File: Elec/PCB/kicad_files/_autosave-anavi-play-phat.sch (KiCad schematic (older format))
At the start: 8 parts

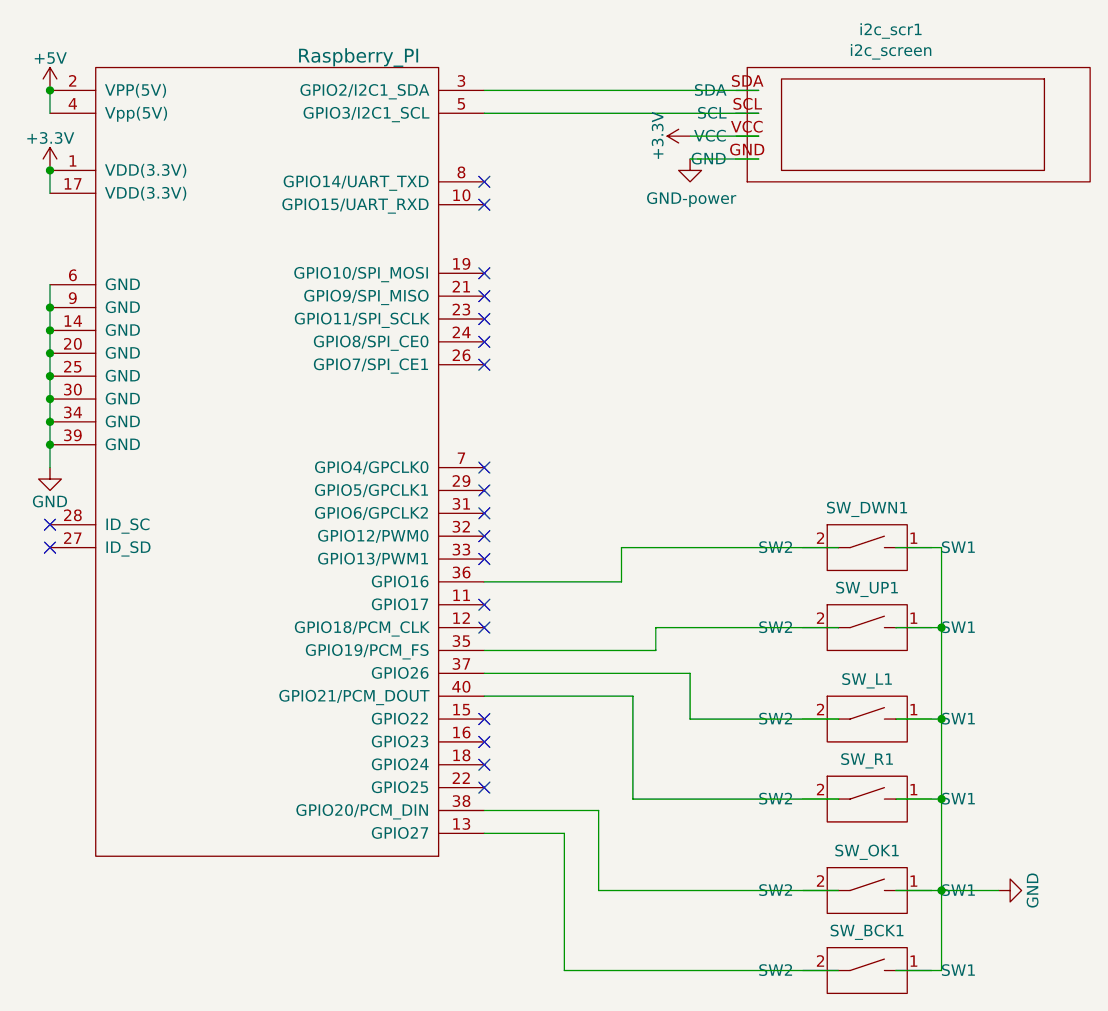
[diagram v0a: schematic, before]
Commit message: PCB v3 correction USB
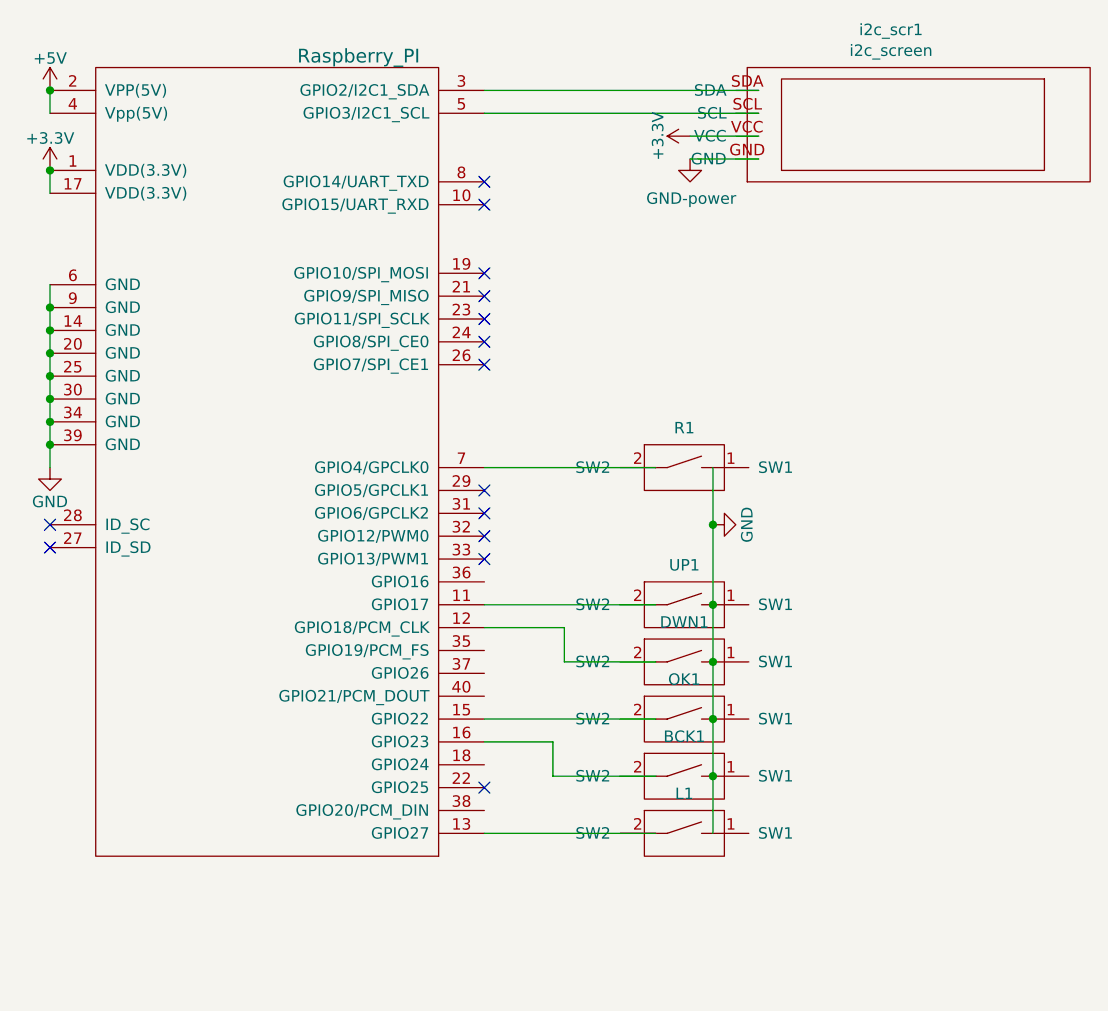
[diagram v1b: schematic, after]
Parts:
- removed SW_BCK1, SW_DWN1, SW_L1, SW_OK1, SW_R1: boutton_5mx5m, boutton:boutton__5mx5m, symbol boutton:boutton_5mx5m
- removed SW_UP1: boutton_5mx5, boutton:boutton__5mx5m, symbol boutton:boutton_5mx5m
- added BCK1, DWN1, L1, OK1, R1, UP1: boutton_6mx6m, boutton:boutton__6mx6m, symbol boutton:boutton_6mx6m
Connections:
- net GND: now also BCK1.1 (SW1), DWN1.1 (SW1), L1.1 (SW1), OK1.1 (SW1), R1.1 (SW1), UP1.1 (SW1)
- net at RASP_CONN1.11 (GPIO17): now also UP1.2 (SW2)
- net at RASP_CONN1.12 (GPIO18/PCM_CLK): now also DWN1.2 (SW2)
- net at RASP_CONN1.13 (GPIO27): now also L1.2 (SW2)
- net at RASP_CONN1.15 (GPIO22): now also OK1.2 (SW2)
- net at RASP_CONN1.16 (GPIO23): now also BCK1.2 (SW2)
- net at RASP_CONN1.7 (GPIO4/GPCLK0): now also R1.2 (SW2)
- no-connect marks 20 -> 14
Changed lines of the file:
@@
 $EndComp
 NoConn ~ 5350 4850
-NoConn ~ 5350 4750
-NoConn ~ 5350 4650
 NoConn ~ 5350 3750
 NoConn ~ 5350 2900
 NoConn ~ 5350 3000
-NoConn ~ 5350 4150
 NoConn ~ 5350 3850
 NoConn ~ 5350 2600
@@
 L anavi-play-phat-rescue:GND-power #PWR016
 U 1 1 5B2D1552
-P 7600 5300
-F 0 "#PWR016" H 7600 5050 50  0001 C CNN
-F 1 "GND" H 7600 5150 50  0000 C CNN
-F 2 "" H 7600 5300 50  0001 C CNN
-F 3 "" H 7600 5300 50  0001 C CNN
-	1    7600 5300
+P 6350 3700
+F 0 "#PWR016" H 6350 3450 50  0001 C CNN
+F 1 "GND" H 6350 3550 50  0000 C CNN
+F 2 "" H 6350 3700 50  0001 C CNN
+F 3 "" H 6350 3700 50  0001 C CNN
+	1    6350 3700
 	0    -1   -1   0
 $EndComp
@@
 	1    0    0    -1
 $EndComp
-Wire Wire Line
-	5350 3950 5950 3950
-Wire Wire Line
-	5950 3950 5950 3800
-Wire Wire Line
-	5950 3800 6900 3800
-Wire Wire Line
-	5350 4250 6100 4250
-Wire Wire Line
-	6100 4250 6100 4150
-Wire Wire Line
-	6100 4150 6900 4150
-Wire Wire Line
-	5350 4950 5850 4950
-Wire Wire Line
-	5850 4950 5850 5300
-Wire Wire Line
-	5850 5300 6900 5300
-Wire Wire Line
-	5350 4350 6250 4350
-Wire Wire Line
-	6250 4350 6250 4550
-Wire Wire Line
-	6250 4550 6900 4550
-Wire Wire Line
-	5350 4450 6000 4450
-Wire Wire Line
-	6000 4450 6000 4900
-Wire Wire Line
-	6000 4900 6900 4900
-Wire Wire Line
-	7150 3800 7350 3800
-Wire Wire Line
-	7350 3800 7350 4150
-Wire Wire Line
-	7350 5300 7600 5300
-Wire Wire Line
-	7150 5300 7350 5300
-Connection ~ 7350 5300
-Wire Wire Line
-	7150 4900 7350 4900
-Connection ~ 7350 4900
-Wire Wire Line
-	7350 4900 7350 5300
-Wire Wire Line
-	7150 4550 7350 4550
-Connection ~ 7350 4550
-Wire Wire Line
-	7350 4550 7350 4900
-Wire Wire Line
-	7150 4150 7350 4150
-Connection ~ 7350 4150
-Wire Wire Line
-	7350 4150 7350 4550
-NoConn ~ 5350 4050
-NoConn ~ 5350 4550
-NoConn ~ 5350 3450
 NoConn ~ 5350 3550
 NoConn ~ 5350 3650
@@
 NoConn ~ 3450 3800
 Wire Wire Line
-	7150 5650 7350 5650
-Wire Wire Line
-	7350 5650 7350 5300
-Wire Wire Line
-	5350 5050 5700 5050
-Wire Wire Line
-	5700 5050 5700 5650
-Wire Wire Line
-	5700 5650 6900 5650
-$Comp
-L boutton:boutton_5mx5m SW_DWN1
-U 1 1 5DD1EB2C
-P 7150 3800
-F 0 "SW_DWN1" H 7025 3973 50  0000 C CNN
-F 1 "boutton_5mx5m" H 7025 3974 50  0001 C CNN
-F 2 "boutton:boutton__5mx5m" H 7150 3700 50  0001 C CNN
-F 3 "" H 7150 3700 50  0001 C CNN
-	1    7150 3800
-	1    0    0    -1
-$EndComp
-$Comp
-L boutton:boutton_5mx5m SW_UP1
-U 1 1 5DD1F4E0
-P 7150 4150
-F 0 "SW_UP1" H 7025 4323 50  0000 C CNN
-F 1 "boutton_5mx5" H 7025 4324 50  0001 C CNN
-F 2 "boutton:boutton__5mx5m" H 7150 4050 50  0001 C CNN
-F 3 "" H 7150 4050 50  0001 C CNN
-	1    7150 4150
-	1    0    0    -1
-$EndComp
-$Comp
-L boutton:boutton_5mx5m SW_L1
-U 1 1 5DD1FF57
-P 7150 4550
-F 0 "SW_L1" H 7025 4723 50  0000 C CNN
-F 1 "boutton_5mx5m" H 7025 4724 50  0001 C CNN
-F 2 "boutton:boutton__5mx5m" H 7150 4450 50  0001 C CNN
-F 3 "" H 7150 4450 50  0001 C CNN
-	1    7150 4550
-	1    0    0    -1
-$EndComp
-$Comp
-L boutton:boutton_5mx5m SW_R1
-U 1 1 5DD20A89
-P 7150 4900
-F 0 "SW_R1" H 7025 5073 50  0000 C CNN
-F 1 "boutton_5mx5m" H 7025 5074 50  0001 C CNN
-F 2 "boutton:boutton__5mx5m" H 7150 4800 50  0001 C CNN
-F 3 "" H 7150 4800 50  0001 C CNN
-	1    7150 4900
-	1    0    0    -1
-$EndComp
-$Comp
-L boutton:boutton_5mx5m SW_OK1
-U 1 1 5DD212C2
-P 7150 5300
-F 0 "SW_OK1" H 7025 5473 50  0000 C CNN
-F 1 "boutton_5mx5m" H 7025 5474 50  0001 C CNN
-F 2 "boutton:boutton__5mx5m" H 7150 5200 50  0001 C CNN
-F 3 "" H 7150 5200 50  0001 C CNN
-	1    7150 5300
-	1    0    0    -1
-$EndComp
-$Comp
-L boutton:boutton_5mx5m SW_BCK1
-U 1 1 5DD21E0C
-P 7150 5650
-F 0 "SW_BCK1" H 7025 5823 50  0000 C CNN
-F 1 "boutton_5mx5m" H 7025 5824 50  0001 C CNN
-F 2 "boutton:boutton__5mx5m" H 7150 5550 50  0001 C CNN
-F 3 "" H 7150 5550 50  0001 C CNN
-	1    7150 5650
-	1    0    0    -1
-$EndComp
+	6350 3450 6350 3700
+$Comp
+L boutton:boutton_6mx6m UP1
+U 1 1 5DE76847
+P 6350 4050
+F 0 "UP1" H 6225 4223 50  0000 C CNN
+F 1 "boutton_6mx6m" H 6200 3900 50  0001 C CNN
+F 2 "boutton:boutton__6mx6m" H 6350 3950 50  0001 C CNN
+F 3 "" H 6350 3950 50  0001 C CNN
+	1    6350 4050
+	1    0    0    -1
+$EndComp
+$Comp
+L boutton:boutton_6mx6m L1
+U 1 1 5DE77762
+P 6350 5050
+F 0 "L1" H 6225 5223 50  0000 C CNN
+F 1 "boutton_6mx6m" H 6200 4900 50  0001 C CNN
+F 2 "boutton:boutton__6mx6m" H 6350 4950 50  0001 C CNN
+F 3 "" H 6350 4950 50  0001 C CNN
+	1    6350 5050
+	1    0    0    -1
+$EndComp
+$Comp
+L boutton:boutton_6mx6m OK1
+U 1 1 5DE79BAE
+P 6350 4550
+F 0 "OK1" H 6225 4723 50  0000 C CNN
+F 1 "boutton_6mx6m" H 6200 4400 50  0001 C CNN
+F 2 "boutton:boutton__6mx6m" H 6350 4450 50  0001 C CNN
+F 3 "" H 6350 4450 50  0001 C CNN
+	1    6350 4550
+	1    0    0    -1
+$EndComp
+$Comp
+L boutton:boutton_6mx6m R1
+U 1 1 5DE7B850
+P 6350 3450
+F 0 "R1" H 6225 3623 50  0000 C CNN
+F 1 "boutton_6mx6m" H 6200 3300 50  0001 C CNN
+F 2 "boutton:boutton__6mx6m" H 6350 3350 50  0001 C CNN
+F 3 "" H 6350 3350 50  0001 C CNN
+	1    6350 3450
+	1    0    0    -1
+$EndComp
+$Comp
+L boutton:boutton_6mx6m DWN1
+U 1 1 5DE7C4F2
+P 6350 4300
+F 0 "DWN1" H 6225 4473 50  0000 C CNN
+F 1 "boutton_6mx6m" H 6200 4150 50  0001 C CNN
+F 2 "boutton:boutton__6mx6m" H 6350 4200 50  0001 C CNN
+F 3 "" H 6350 4200 50  0001 C CNN
+	1    6350 4300
+	1    0    0    -1
+$EndComp
+$Comp
+L boutton:boutton_6mx6m BCK1
+U 1 1 5DE7DEC3
+P 6350 4800
+F 0 "BCK1" H 6225 4973 50  0000 C CNN
+F 1 "boutton_6mx6m" H 6200 4650 50  0001 C CNN
+F 2 "boutton:boutton__6mx6m" H 6350 4700 50  0001 C CNN
+F 3 "" H 6350 4700 50  0001 C CNN
+	1    6350 4800
+	1    0    0    -1
+$EndComp
+Wire Wire Line
+	5350 3450 6100 3450
+Wire Wire Line
+	5350 4050 6100 4050
+Wire Wire Line
+	5350 4150 5700 4150
+Wire Wire Line
+	5700 4150 5700 4300
+Wire Wire Line
+	5700 4300 6100 4300
+Wire Wire Line
+	5350 4550 6100 4550
+Wire Wire Line
+	5350 4650 5650 4650
+Wire Wire Line
+	5650 4650 5650 4800
+Wire Wire Line
+	5650 4800 6100 4800
+Wire Wire Line
+	5350 5050 6100 5050
+Connection ~ 6350 4050
+Wire Wire Line
+	6350 4050 6350 4300
+Connection ~ 6350 4300
+Wire Wire Line
+	6350 4300 6350 4550
+Connection ~ 6350 4550
+Wire Wire Line
+	6350 4550 6350 4800
+Connection ~ 6350 4800
+Wire Wire Line
+	6350 4800 6350 5050
+Connection ~ 6350 3700
+Wire Wire Line
+	6350 3700 6350 4050
 $EndSCHEMATC
